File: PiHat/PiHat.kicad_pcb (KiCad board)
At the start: 2 copper layers, 65 x 56 mm, 33 parts, among them J1 Raspberry_Pi_2_3, J2 PWR_IN, J3 VIN Voltage, J4 String 1, J5 String 2, J6 RTC Conn, J7 DMX Out, J8 OLED, J9 GPIO, U1 74HC125, U2 OKI-78SR-5, U3 SP3485CP

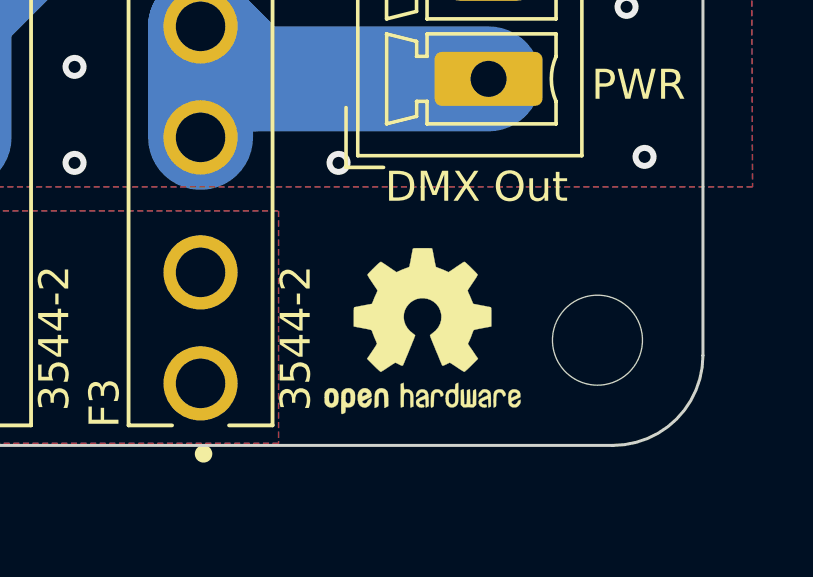
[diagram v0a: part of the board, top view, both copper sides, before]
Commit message: added BOM and Added serial port silkscreen
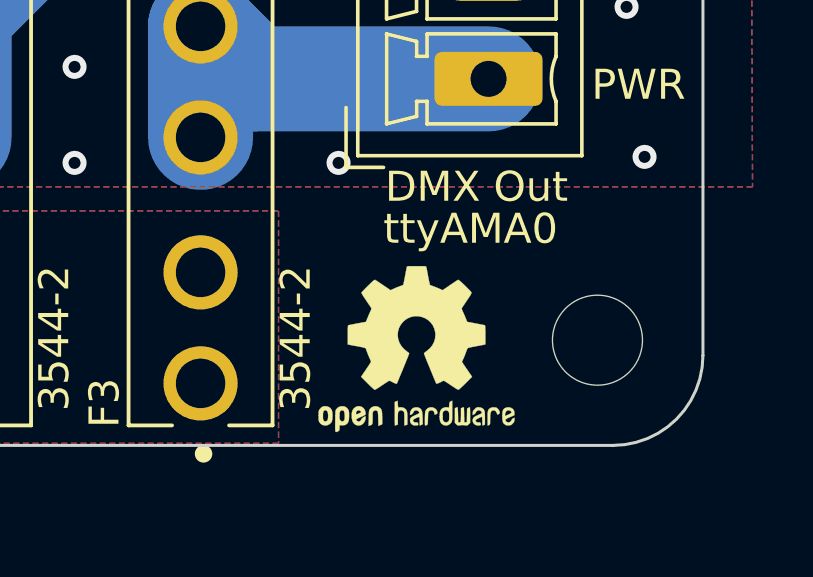
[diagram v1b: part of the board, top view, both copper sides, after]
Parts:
- moved REF** 0.63 mm to (134.0, 113.6)
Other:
- board text added: "ttyAMA0"

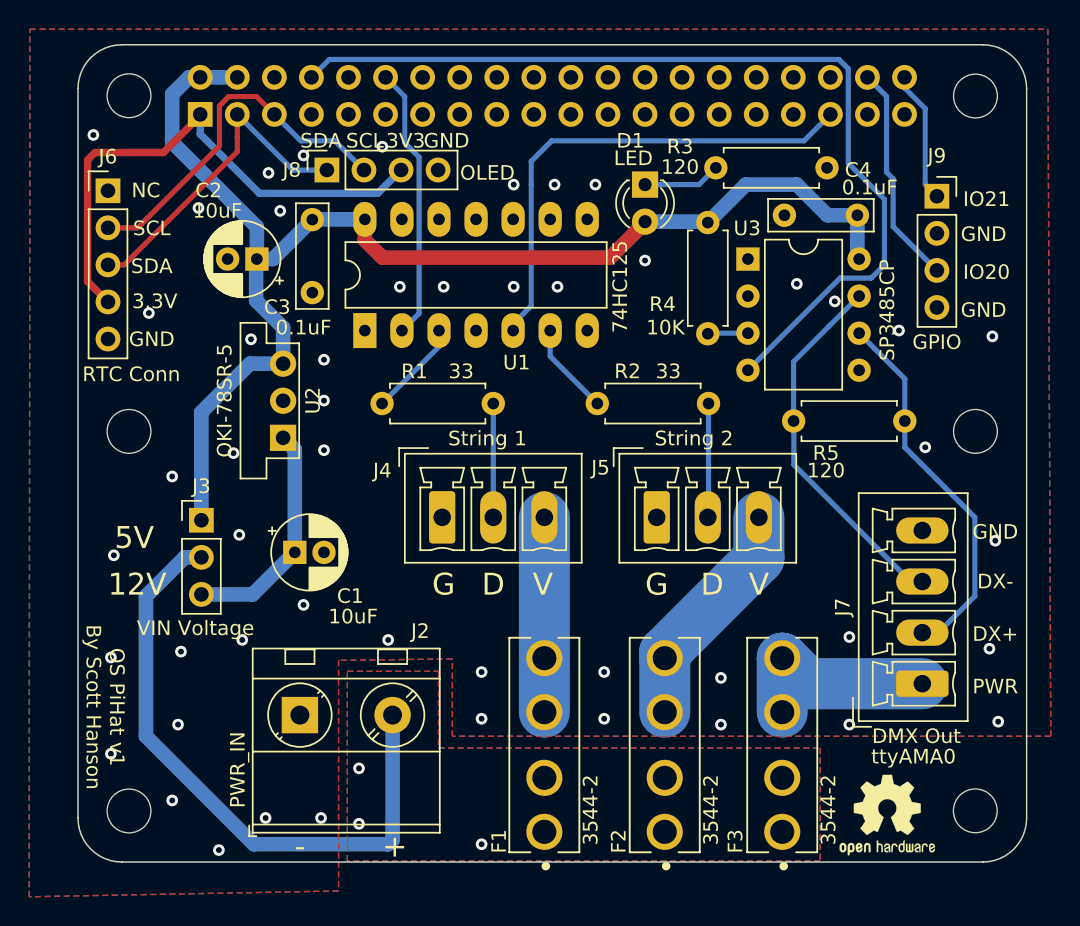
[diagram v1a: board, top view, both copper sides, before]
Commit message: add plug in 3 to 4 adapter
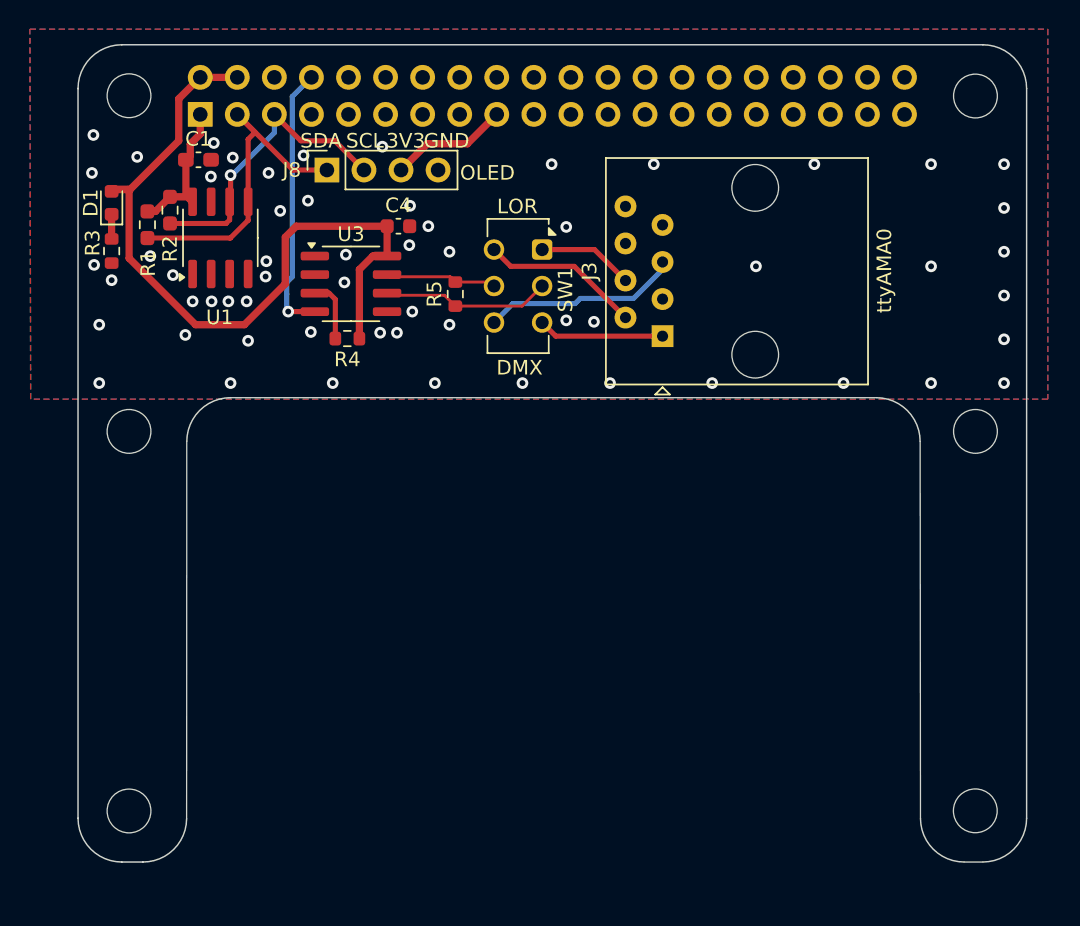
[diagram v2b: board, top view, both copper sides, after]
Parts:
- removed C2: 10uF, Capacitor_THT:CP_Radial_D5.0mm_P2.00mm
- removed C3: 0.1uF, Capacitor_THT:C_Rect_L7.0mm_W2.0mm_P5.00mm
- removed F1, F2, F3: 3544-2, Keystone_Fuse:FUSE_3544-2
- removed J2: PWR_IN, TerminalBlock_MetzConnect:TerminalBlock_MetzConnect_Type701_RT11L02HGLU_1x02_P6.35mm_Horizontal
- removed J4: String 1, Connector_Phoenix_MC:PhoenixContact_MCV_1,5_3-G-3.5_1x03_P3.50mm_Vertical
- removed J5: String 2, Connector_Phoenix_MC:PhoenixContact_MCV_1,5_3-G-3.5_1x03_P3.50mm_Vertical
- removed J6: RTC Conn, Connector_PinHeader_2.54mm:PinHeader_1x05_P2.54mm_Vertical
- removed J7: DMX Out, Connector_Phoenix_MC:PhoenixContact_MCV_1,5_4-G-3.5_1x04_P3.50mm_Vertical
- removed J9: GPIO, Connector_PinSocket_2.54mm:PinSocket_1x04_P2.54mm_Vertical
- removed REF**: OSHW-Logo2_7.3x6mm_SilkScreen, Symbol:OSHW-Logo2_7.3x6mm_SilkScreen
- removed REF**: KiCad-Logo2_5mm_SilkScreen, Symbol:KiCad-Logo2_5mm_SilkScreen
- removed U2: OKI-78SR-5, Converter_DCDC:Converter_DCDC_muRata_OKI-78SR_Vertical
- added SW1: DMX_LOR_Select, Button_Switch_THT:SW_CK_JS202011CQN_DPDT_Straight, F.Cu at (110.3, 74.8)
- C1: value 10uF -> 0.1uF; footprint Capacitor_THT:CP_Radial_D5.0mm_P2.00mm -> Capacitor_SMD:C_0603_1608Metric_Pad1.08x0.95mm_HandSolder
- C4: footprint Capacitor_THT:C_Rect_L7.0mm_W2.0mm_P5.00mm -> Capacitor_SMD:C_0603_1608Metric
- D1: footprint LED_THT:LED_D3.0mm_Clear -> LED_SMD:LED_0603_1608Metric
- J3: value VIN Voltage -> DMX1 RJ45; footprint Connector_PinHeader_2.54mm:PinHeader_1x03_P2.54mm_Vertical -> Connector_RJ:RJ45_Amphenol_54602-x08_Horizontal
- R1, R2: value 33 -> 4.7K; footprint Resistor_THT:R_Axial_DIN0207_L6.3mm_D2.5mm_P7.62mm_Horizontal -> Resistor_SMD:R_0603_1608Metric_Pad0.98x0.95mm_HandSolder
- R3, R4, R5: footprint Resistor_THT:R_Axial_DIN0207_L6.3mm_D2.5mm_P7.62mm_Horizontal -> Resistor_SMD:R_0603_1608Metric
- U1: value 74HC125 -> 24LC256; footprint Package_DIP:DIP-14_W7.62mm_LongPads -> Package_SO:SOIC-8_3.9x4.9mm_P1.27mm
- U3: footprint Package_DIP:DIP-8_W7.62mm -> Package_SO:SOIC-8_3.9x4.9mm_P1.27mm
- moved R3 41.8 mm to (80.8, 75.0), turned to -90 degrees
- moved R2 39.2 mm to (84.8, 72.2), turned to 90 degrees
- moved D1 36.6 mm to (80.8, 71.7), turned to 90 degrees
- moved J3 34.0 mm to (118.6, 80.8), turned to 90 degrees
- moved R5 32.0 mm to (104.4, 77.9), turned to 90 degrees
- moved C4 31.5 mm to (100.5, 73.2), turned to 0 degrees
- moved C1 27.7 mm to (86.8, 68.7)
- moved U3 27.3 mm to (97.2, 77.2)
- moved R1 26.7 mm to (83.3, 73.2), turned to 90 degrees
- moved R4 25.9 mm to (97.0, 81.0), turned to 180 degrees
- moved U1 11.8 mm to (88.3, 74.0)
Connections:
- C1 pad 1: /PWR_IN -> +3.3V
- J1 pad 1: +3V3 -> +3.3V
- J1 pad 10: Net-(J1-Pad10) -> unconnected-(J1-GPIO15/RXD-Pad10)
- J1 pad 11: Net-(J1-Pad11) -> unconnected-(J1-GPIO17-Pad11)
- J1 pad 12: Pixel1 -> unconnected-(J1-GPIO18/PWM0-Pad12)
- J1 pad 13: Net-(J1-Pad13) -> unconnected-(J1-GPIO27-Pad13)
- J1 pad 15: Net-(J1-Pad15) -> unconnected-(J1-GPIO22-Pad15)
- J1 pad 16: Net-(J1-Pad16) -> unconnected-(J1-GPIO23-Pad16)
- J1 pad 17: Net-(J1-Pad17) -> +3.3V
- J1 pad 18: Net-(J1-Pad18) -> unconnected-(J1-GPIO24-Pad18)
- J1 pad 19: Net-(J1-Pad19) -> unconnected-(J1-MOSI0/GPIO10-Pad19)
- J1 pad 21: Net-(J1-Pad21) -> unconnected-(J1-MISO0/GPIO9-Pad21)
- J1 pad 22: Net-(J1-Pad22) -> unconnected-(J1-GPIO25-Pad22)
- J1 pad 23: Net-(J1-Pad23) -> unconnected-(J1-SCLK0/GPIO11-Pad23)
- J1 pad 24: Net-(J1-Pad24) -> unconnected-(J1-~{CE0}/GPIO8-Pad24)
- J1 pad 26: Net-(J1-Pad26) -> unconnected-(J1-~{CE1}/GPIO7-Pad26)
- J1 pad 27: Net-(J1-Pad27) -> unconnected-(J1-ID_SD/GPIO0-Pad27)
- J1 pad 28: Net-(J1-Pad28) -> unconnected-(J1-ID_SC/GPIO1-Pad28)
- J1 pad 29: Net-(J1-Pad29) -> unconnected-(J1-GCLK1/GPIO5-Pad29)
- J1 pad 31: Net-(J1-Pad31) -> unconnected-(J1-GCLK2/GPIO6-Pad31)
- J1 pad 32: Net-(J1-Pad32) -> unconnected-(J1-PWM0/GPIO12-Pad32)
- J1 pad 33: Net-(J1-Pad33) -> unconnected-(J1-PWM1/GPIO13-Pad33)
- J1 pad 35: Pixel2 -> unconnected-(J1-GPIO19/MISO1-Pad35)
- J1 pad 36: Net-(J1-Pad36) -> unconnected-(J1-GPIO16-Pad36)
- J1 pad 37: Net-(J1-Pad37) -> unconnected-(J1-GPIO26-Pad37)
- J1 pad 7: Net-(J1-Pad7) -> unconnected-(J1-GCLK0/GPIO4-Pad7)
- J3 pad 1: +5V -> Net-(SW1A-C)
- J3 pad 2: VSS -> Net-(SW1B-C)
- J3 pad 3: /PWR_IN -> /9V
- J8 pad 3: +3V3 -> +3.3V
- R1 pad 1: Net-(J4-Pad2) -> I2C_SDA
- R1 pad 2: Net-(R1-Pad2) -> +3.3V
- R2 pad 1: Net-(J5-Pad2) -> I2C_SCL
- R2 pad 2: Net-(R2-Pad2) -> +3.3V
- U1 pad 2: Pixel1 -> GND
- U1 pad 3: Net-(R1-Pad2) -> GND
- U1 pad 5: Pixel2 -> I2C_SDA
- U1 pad 6: Net-(R2-Pad2) -> I2C_SCL
- U1 pad 8: Net-(U1-Pad8) -> +3.3V
- U3 pad 1: Net-(U3-Pad1) -> unconnected-(U3-RO-Pad1)
- U3 pad 2: Net-(U3-Pad2) -> unconnected-(U3-~{RE}-Pad2)
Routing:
- net TXD: track 64.4 -> 18.6 mm, vias 0 -> 1
- net VSS: track 43.1 -> 0.00 mm, vias 3 -> 0
- net +5V: track 91.2 -> 53.1 mm
- net +3V3: track 36.8 -> 0.00 mm
- net Pixel2: track 33.9 -> 0.00 mm
- net Pixel1: track 18.8 -> 0.00 mm
- net +3.3V: track 0.00 -> 18.4 mm
- net /DMX-: track 25.5 -> 7.65 mm
- net /ST2_PWR: track 16.0 -> 0.00 mm
- net /PWR_IN: track 15.8 -> 0.00 mm
- net GPIO20: track 15.2 -> 0.00 mm
- net /DMX+: track 25.9 -> 11.6 mm
- net /V_DMX: track 14.0 -> 0.00 mm
- net Net-(SW1B-A): track 0.00 -> 13.6 mm
- net /ST1_PWR: track 13.3 -> 0.00 mm
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- removed copper zone on B.Cu, net VSS
- removed copper zone on F.Cu, net VSS
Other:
- outline, holes or cut-outs redrawn
- net class 3.3V removed
- net class 5V removed
- net class Default removed
- net class PWR removed
- board text added: "DMX"
- board text added: "LOR"
- board text removed: "+"
- board text removed: "-"
- board text removed: "12V"
- board text removed: "3.3V"
- board text removed: "5V"
- board text removed: "D"
- board text removed: "DX+"
- board text removed: "DX-"
- board text removed: "G"
- board text removed: "IO20"
- board text removed: "IO21"
- board text removed: "NC"
- board text removed: "OS PiHat v1 By Scott Hanson"
- board text removed: "PWR"
- board text removed: "V"
